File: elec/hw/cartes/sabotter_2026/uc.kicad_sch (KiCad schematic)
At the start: 34 parts, among them J3 USB4105-GF-A-060, SW1 TSB001A3526A02, U3 ESP32-S3-WROOM-1

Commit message: sabotter wip
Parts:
- added R65: 0R, cocotter_resistor:r0603_reflow, symbol cocotter_resistors:R_0R_0603
- added TP7, TP8: TestPoint, cocotter_others:testpoint-THT-0.5mm, symbol cocotter_others:TestPoint
- J3: value USB4105-GF-A-060 -> USB4120-03-C; footprint cocotter_connectors:USB4105 -> cocotter_connectors:USB4120-03-C; symbol cocotter_connectors:USB-TYPE-C-019 -> cocotter_connectors:USB4120-03-C; DIGIKEY_REF 2073-USB4105-GF-A-060TR-ND -> (none); JLC (none) -> C7450621; JLCPCB Part # C2927039 -> (none)
- SW1: value TSB001A3526A02 -> PTS525 SK15 SMTR2 LFS; footprint cocotter_others:TSB001A3526A02 -> cocotter_others:PTS525 SK15 SMTR2 LFS; symbol cocotter_others:TSB001A3526A02 -> cocotter_others:PTS525 SK15 SMTR2 LFS; JLCPCB Part # C2888889 -> C2689599
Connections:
- net EN_ESP32_3v3: now also R65.2; no longer SW1.2
- net GND: now also SW1.A (1); no longer SW1.1, SW1.MP
- net scl_3v3: now also TP8.1
- net sda_3v3: now also TP7.1
- new net: R65.1, SW1.B (2)

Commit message: sabotter wip
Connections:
- net encod_mot0_A_3v3: now also U3.28 (IO35,SPIIO6,GPIO35,FSPID,SUBSPID); no longer U3.32 (IO39,MTCK,GPIO39,CLK_OUT3,SUBSPICS1)
- net encod_mot0_B_3v3: now also U3.17 (IO9,RTC_GPIO9,GPIO9,TOUCH9,ADC1_CH8,FSPIHD,SUBSPIHD); no longer U3.33 (IO40,MTDO,GPIO40,CLK_OUT2)
- net encod_mot1_A_3v3: now also U3.18 (IO10,RTC_GPIO10,GPIO10,TOUCH10,ADC1_CH9,FSPICS0,FSPIIO4,SUBSPICS0); no longer U3.34 (IO41,MTDI,GPIO41,CLK_OUT1)
- net encod_mot1_B_3v3: now also U3.15 (IO3,RTC_GPIO3,GPIO3,TOUCH3,ADC1_CH2); no longer U3.35 (IO42,MTMS,GPIO42)
- net gyro_miso_3v3: now also U3.30 (IO37,SPIDQS,GPIO37,FSPIQ,SUBSPIQ); no longer U3.28 (IO35,SPIIO6,GPIO35,FSPID,SUBSPID)
- net gyro_mosi_3v3: now also U3.31 (IO38,GPIO38,FSPIWP,SUBSPIWP); no longer U3.29 (IO36,SPIIO7,GPIO36,FSPICLK,SUBSPICL)
- net gyro_sck_3v3: now also U3.32 (IO39,MTCK,GPIO39,CLK_OUT3,SUBSPICS1); no longer U3.31 (IO38,GPIO38,FSPIWP,SUBSPIWP)
- net lidar_pwm_3v3: now also U3.35 (IO42,MTMS,GPIO42); no longer U3.15 (IO3,RTC_GPIO3,GPIO3,TOUCH3,ADC1_CH2)
- net scl_3v3: now also U3.34 (IO41,MTDI,GPIO41,CLK_OUT1); no longer U3.18 (IO10,RTC_GPIO10,GPIO10,TOUCH10,ADC1_CH9,FSPICS0,FSPIIO4,SUBSPICS0)
- net sda_3v3: now also U3.33 (IO40,MTDO,GPIO40,CLK_OUT2); no longer U3.17 (IO9,RTC_GPIO9,GPIO9,TOUCH9,ADC1_CH8,FSPIHD,SUBSPIHD)
- net /gyro_cs_3v3: now also U3.29 (IO36,SPIIO7,GPIO36,FSPICLK,SUBSPICL); no longer U3.30 (IO37,SPIDQS,GPIO37,FSPIQ,SUBSPIQ)
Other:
- moved on the sheet: R10, R21, R5, R6, R9, TP7, TP8

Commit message: sabotter ready for first schematic and routing review
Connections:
- net can_rx_3v3: now also U3.18 (IO10,RTC_GPIO10,GPIO10,TOUCH10,ADC1_CH9,FSPICS0,FSPIIO4,SUBSPICS0); no longer U3.19 (IO11,RTC_GPIO11,GPIO11,TOUCH11,FSPID,FSPIIO5,SUBSPID)
- net can_tx_3v3: now also U3.17 (IO9,RTC_GPIO9,GPIO9,TOUCH9,ADC1_CH8,FSPIHD,SUBSPIHD); no longer U3.12 (IO8,RTC_GPIO8,GPIO8,TOUCH8,ADC1_CH7,SUBSPICS1)
- net dir_mot0_3v3: now also U3.11 (IO18,RTC_GPIO18,GPIO18,U1RXD,CLK_OUT3); no longer U3.20 (IO12,RTC_GPIO12,GPIO12,TOUCH12,FSPICLK,FSPIIO6,SUBSPICLK)
- net dir_mot1_3v3: now also U3.12 (IO8,RTC_GPIO8,GPIO8,TOUCH8,ADC1_CH7,SUBSPICS1); no longer U3.22 (IO14,RTC_GPIO14,GPIO14,TOUCH14,FSPIWP,FSPIDQS,SUBSPIWP)
- net dir_mot2_3v3: now also U3.25 (IO48,SPICLK_N_DIFF,GPIO48,SUBSPICLK_N_DIFF); no longer U3.9 (IO16,RTC_GPIO16,GPIO16,U0CTS,XTAL_32K_N)
- net encod_mot0_A_3v3: now also U3.19 (IO11,RTC_GPIO11,GPIO11,TOUCH11,FSPID,FSPIIO5,SUBSPID); no longer U3.28 (IO35,SPIIO6,GPIO35,FSPID,SUBSPID)
- net encod_mot0_B_3v3: now also U3.20 (IO12,RTC_GPIO12,GPIO12,TOUCH12,FSPICLK,FSPIIO6,SUBSPICLK); no longer U3.17 (IO9,RTC_GPIO9,GPIO9,TOUCH9,ADC1_CH8,FSPIHD,SUBSPIHD)
- net encod_mot1_A_3v3: now also U3.9 (IO16,RTC_GPIO16,GPIO16,U0CTS,XTAL_32K_N); no longer U3.18 (IO10,RTC_GPIO10,GPIO10,TOUCH10,ADC1_CH9,FSPICS0,FSPIIO4,SUBSPICS0)
- net encod_mot1_B_3v3: now also U3.8 (IO15,RTC_GPIO15,GPIO15,U0RTS,XTAL_32K_P); no longer U3.15 (IO3,RTC_GPIO3,GPIO3,TOUCH3,ADC1_CH2)
- net encod_mot2_A_3v3: now also U3.22 (IO14,RTC_GPIO14,GPIO14,TOUCH14,FSPIWP,FSPIDQS,SUBSPIWP); no longer U3.24 (IO47,SPICLK_P_DIFF,GPIO47,SUBSPICLK_P_DIFF)
- net encod_mot2_B_3v3: now also U3.21 (IO13,RTC_GPIO13,GPIO13,TOUCH13,FSPIQ,FSPIIO7,SUBSPIQ); no longer U3.25 (IO48,SPICLK_N_DIFF,GPIO48,SUBSPICLK_N_DIFF)
- net pwm_mot0_3v3: now also U3.10 (IO17,RTC_GPIO17,GPIO17,U1TXD); no longer U3.21 (IO13,RTC_GPIO13,GPIO13,TOUCH13,FSPIQ,FSPIIO7,SUBSPIQ)
- net pwm_mot1_3v3: now also U3.15 (IO3,RTC_GPIO3,GPIO3,TOUCH3,ADC1_CH2); no longer U3.8 (IO15,RTC_GPIO15,GPIO15,U0RTS,XTAL_32K_P)
- net pwm_mot2_3v3: now also U3.28 (IO35,SPIIO6,GPIO35,FSPID,SUBSPID); no longer U3.23 (IO21,RTC_GPIO21,GPIO21)
- net scl_tof_3v3: now also U3.24 (IO47,SPICLK_P_DIFF,GPIO47,SUBSPICLK_P_DIFF); no longer U3.11 (IO18,RTC_GPIO18,GPIO18,U1RXD,CLK_OUT3)
- net sda_tof_3v3: now also U3.23 (IO21,RTC_GPIO21,GPIO21); no longer U3.10 (IO17,RTC_GPIO17,GPIO17,U1TXD)
- net tx_to_prop_3v3: now also U3.6 (IO6,RTC_GPIO6,GPIO6,TOUCH6,ADC1_CH5); no longer U3.4 (IO4,RTC_GPIO4,GPIO4,TOUCH4,ADC1_CH3)
- net ws2812_data_3v3: now also U3.4 (IO4,RTC_GPIO4,GPIO4,TOUCH4,ADC1_CH3); no longer U3.6 (IO6,RTC_GPIO6,GPIO6,TOUCH6,ADC1_CH5)
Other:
- moved on the sheet: R10, R11, R12, R14, R15, R5, R6, R7, R8, R9, TP1, TP2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

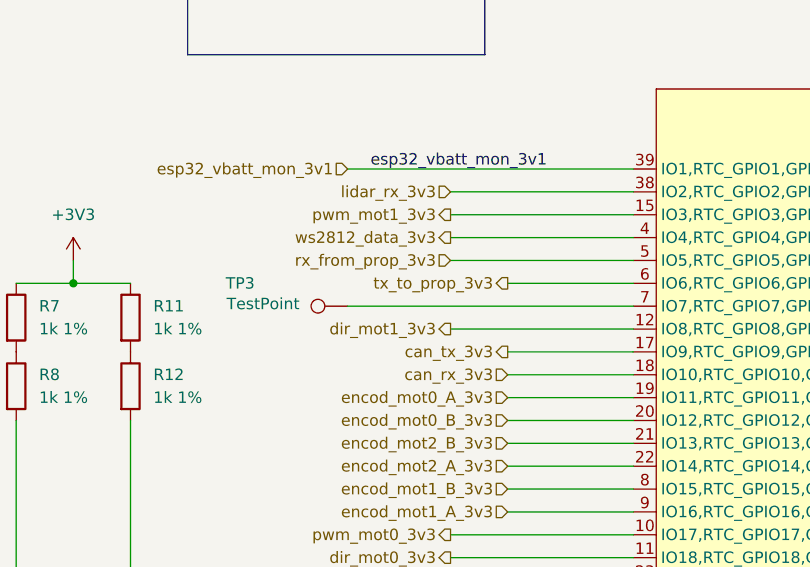
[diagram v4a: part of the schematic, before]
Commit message: tof irq added, needs routing
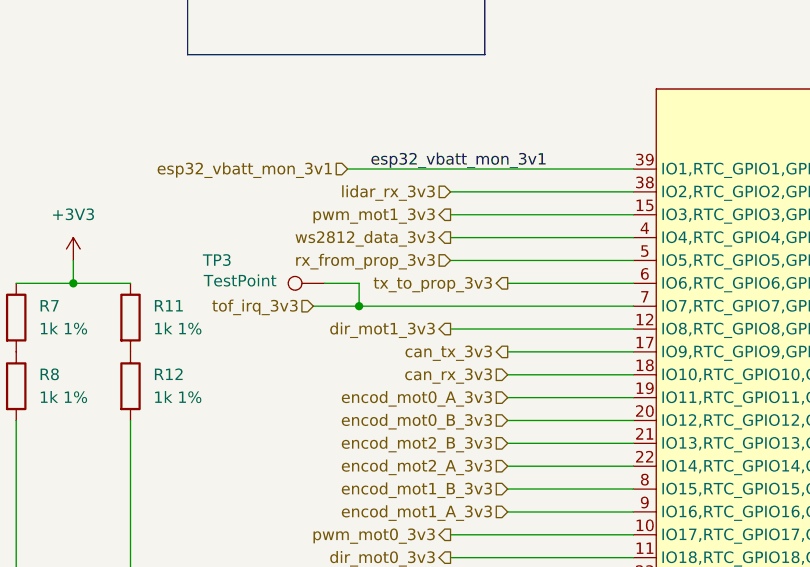
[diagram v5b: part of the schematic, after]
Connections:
- net tof_irq_3v3: now reaches TP3.1, U3.7 (IO7,RTC_GPIO7,GPIO7,TOUCH7,ADC1_CH6)
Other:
- moved on the sheet: TP3
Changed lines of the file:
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@@
 	)
 	(junction
+		(at 104.14 71.12)
+		(diameter 0)
+		(color 0 0 0 0)
+	)
+	(junction
 		(at 30.48 104.14)
 		(diameter 0)
@@
 	(wire
 		(pts
+			(xy 104.14 71.12) (xy 134.62 71.12)
+		)
+		(stroke
+			(width 0)
+			(type default)
+		)
+	)
+	(wire
+		(pts
 			(xy 52.07 100.33) (xy 52.07 101.6)
 		)
@@
 	(wire
 		(pts
+			(xy 99.06 71.12) (xy 104.14 71.12)
+		)
+		(stroke
+			(width 0)
+			(type default)
+		)
+	)
+	(wire
+		(pts
 			(xy 135.89 176.53) (xy 124.46 176.53)
 		)
@@
 	(wire
 		(pts
-			(xy 102.87 71.12) (xy 134.62 71.12)
+			(xy 100.33 68.58) (xy 104.14 68.58)
 		)
 		(stroke
@@
 	(wire
 		(pts
+			(xy 104.14 68.58) (xy 104.14 71.12)
+		)
+		(stroke
+			(width 0)
+			(type default)
+		)
+	)
+	(wire
+		(pts
 			(xy 172.72 148.59) (xy 172.72 149.86)
 		)
@@
 		)
 	)
+	(hierarchical_label "tof_irq_3v3"
+		(shape input)
+		(at 99.06 71.12 180)
+		(effects
+			(font
+				(size 1.27 1.27)
+			)
+			(justify right)
+		)
+	)
 	(hierarchical_label "encod_mot0_A_3v3"
 		(shape input)
@@
 	(symbol
 		(lib_id "cocotter_others:TestPoint")
-		(at 102.87 71.12 90)
+		(at 100.33 68.58 90)
 		(unit 1)
 		(exclude_from_sim no)
@@
 		(dnp no)
 		(property "Reference" "TP3"
-			(at 90.932 68.58 90)
+			(at 88.392 66.04 90)
 			(effects
 				(font
@@
 		)
 		(property "Value" "TestPoint"
-			(at 93.472 70.866 90)
+			(at 90.932 68.326 90)
 			(effects
 				(font
@@
 		)
 		(property "Footprint" "cocotter_others:testpoint-THT-0.5mm"
-			(at 102.87 66.04 0)
+			(at 100.33 63.5 0)
 			(effects
 				(font
@@
 		)
 		(property "Datasheet" "~"
-			(at 102.87 66.04 0)
+			(at 100.33 63.5 0)
 			(effects
 				(font
@@
 		)
 		(property "Description" "test point"
-			(at 102.87 71.12 0)
+			(at 100.33 68.58 0)
 			(effects
 				(font

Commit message: sabotter corrections wip
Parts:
- removed R65: 0R, cocotter_resistor:r0603_reflow, symbol cocotter_resistors:R_0R_0603
- added SW2: SLW-713515-2A-SMT-TR, cocotter_others:SLW-713515-2A-SMT-TR, symbol cocotter_connectors:SLW-713515-2A-SMT-TR
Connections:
- net EN_ESP32_3v3: now also SW2.2
- net at SW1.B (2): now also SW2.1
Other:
- moved on the sheet: SW1
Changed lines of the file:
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@@
 	(wire
 		(pts
-			(xy 69.85 152.4) (xy 69.85 153.67)
+			(xy 57.15 152.4) (xy 57.15 153.67)
 		)
 		(stroke
@@
 	(wire
 		(pts
+			(xy 73.66 143.51) (xy 80.01 143.51)
+		)
+		(stroke
+			(width 0)
+			(type default)
+		)
+	)
+	(wire
+		(pts
 			(xy 231.14 149.86) (xy 231.14 151.13)
 		)
@@
 	(wire
 		(pts
-			(xy 69.85 143.51) (xy 69.85 144.78)
+			(xy 57.15 140.97) (xy 57.15 144.78)
 		)
 		(stroke
@@
 	(wire
 		(pts
-			(xy 78.74 143.51) (xy 80.01 143.51)
-		)
-		(stroke
-			(width 0)
-			(type default)
-		)
-	)
-	(wire
-		(pts
 			(xy 104.14 68.58) (xy 104.14 71.12)
 		)
@@
 	(wire
 		(pts
-			(xy 69.85 143.51) (xy 71.12 143.51)
+			(xy 57.15 140.97) (xy 63.5 140.97)
 		)
 		(stroke
@@
 	)
 	(symbol
-		(lib_id "cocotter_resistors:R_0R_0603")
-		(at 74.93 143.51 90)
-		(unit 1)
-		(exclude_from_sim no)
-		(in_bom yes)
-		(on_board yes)
-		(dnp no)
-		(fields_autoplaced yes)
-		(property "Reference" "R65"
-			(at 74.93 137.16 90)
-			(effects
-				(font
-					(size 1.27 1.27)
-				)
-			)
-		)
-		(property "Value" "0R"
-			(at 74.93 139.7 90)
-			(effects
-				(font
-					(size 1.27 1.27)
-				)
-			)
-		)
-		(property "Footprint" "cocotter_resistor:r0603_reflow"
-			(at 74.93 145.288 90)
-			(effects
-				(font
-					(size 1.27 1.27)
-				)
-				(hide yes)
-			)
-		)
-		(property "Datasheet" "~"
-			(at 74.93 143.51 0)
-			(effects
-				(font
-					(size 1.27 1.27)
-				)
-				(hide yes)
-			)
-		)
-		(property "Description" "Resistor"
-			(at 74.93 143.51 0)
-			(effects
-				(font
-					(size 1.27 1.27)
-				)
-				(hide yes)
-			)
-		)
-		(property "Specification" "0R 0603 20mOhms max 100mW"
-			(at 74.93 143.51 0)
-			(effects
-				(font
-					(size 1.27 1.27)
-				)
-				(hide yes)
-			)
-		)
-		(property "mouser" ""
-			(at 74.93 143.51 0)
-			(effects
-				(font
-					(size 1.27 1.27)
-				)
-				(hide yes)
-			)
-		)
-		(property "JLCPCB Part #" "C431718"
-			(at 74.93 143.51 0)
-			(effects
-				(font
-					(size 1.27 1.27)
-				)
-				(hide yes)
-			)
-		)
-		(pin "1"
-		)
-		(pin "2"
-		)
-		(instances
-			(project ""
-				(path "/c1bd5504-d0b2-4cc3-94d1-261f58816249/0627c134-32e1-430c-bbd1-677b8ecf53c1"
-					(reference "R65")
-					(unit 1)
-				)
-			)
-		)
-	)
-	(symbol
 		(lib_id "pmi_2023_specific:+3V3_m")
 		(at 72.39 66.04 0)
@@
 	(symbol
 		(lib_id "cocotter_others:PTS525 SK15 SMTR2 LFS")
-		(at 69.85 148.59 90)
+		(at 57.15 148.59 90)
 		(unit 1)
 		(exclude_from_sim no)
@@
 		(dnp no)
 		(property "Reference" "SW1"
-			(at 65.278 148.59 0)
+			(at 52.578 148.59 0)
 			(effects
 				(font
@@
 		)
 		(property "Value" "PTS525 SK15 SMTR2 LFS"
-			(at 74.93 146.05 0)
+			(at 62.23 146.05 0)
 			(effects
 				(font
@@
 		)
 		(property "Footprint" "cocotter_others:PTS525 SK15 SMTR2 LFS"
-			(at 69.85 148.59 0)
+			(at 57.15 148.59 0)
 			(effects
 				(font
@@
 		)
 		(property "Datasheet" ""
-			(at 74.93 148.59 0)
+			(at 62.23 148.59 0)
 			(effects
 				(font
@@
 		)
 		(property "Description" "20mA max, 15Vdc, 100mohms max, 500k cycle, 260gf"
-			(at 69.85 148.59 0)
+			(at 57.15 148.59 0)
 			(effects
 				(font
@@
 		)
 		(property "JLCPCB Part #" "C2689599"
-			(at 74.93 149.86 0)
+			(at 62.23 149.86 0)
 			(effects
 				(font
@@
 	)
 	(symbol
+		(lib_id "cocotter_connectors:SLW-713515-2A-SMT-TR ")
+		(at 68.58 143.51 0)
+		(unit 1)
+		(exclude_from_sim no)
+		(in_bom yes)
+		(on_board yes)
+		(dnp no)
+		(fields_autoplaced yes)
+		(property "Reference" "SW2"
+			(at 68.58 134.62 0)
+			(effects
+				(font
+					(size 1.27 1.27)
+				)
+			)
+		)
+		(property "Value" "SLW-713515-2A-SMT-TR"
+			(at 68.58 137.16 0)
+			(effects
+				(font
+					(size 1.27 1.27)
+				)
+			)
+		)
+		(property "Footprint" "cocotter_others:SLW-713515-2A-SMT-TR"
+			(at 68.58 143.51 0)
+			(effects
+				(font
+					(size 1.27 1.27)
+				)
+				(hide yes)
+			)
+		)
+		(property "Datasheet" "https://www.sameskydevices.com/product/resource/slw-713515-2a-smt-tr.pdf"
+			(at 68.58 148.59 0)
+			(effects
+				(font
+					(size 1.27 1.27)
+				)
+				(hide yes)
+			)
+		)
+		(property "Description" "50mA max, 12Vdc, 10000 cycles"
+			(at 68.58 143.51 0)
+			(effects
+				(font
+					(size 1.27 1.27)
+				)
+				(hide yes)
+			)
+		)
+		(property "JLCPCB Part #" "C2858291"
+			(at 67.31 148.59 0)
+			(effects
+				(font
+					(size 1.27 1.27)
+				)
+				(hide yes)
+			)
+		)
+		(pin "2"
+		)
+		(pin "1"
+		)
+		(pin "3"
+		)
+		(pin "6"
+		)
+		(pin "4"
+		)
+		(pin "5"
+		)
+		(instances
+			(project ""
+				(path "/c1bd5504-d0b2-4cc3-94d1-261f58816249/0627c134-32e1-430c-bbd1-677b8ecf53c1"
+					(reference "SW2")
+					(unit 1)
+				)
+			)
+		)
+	)
+	(symbol
 		(lib_id "cocotter_resistors:R_0R_0603")
 		(at 120.65 173.99 90)
@@
 	(symbol
 		(lib_id "pmi_2023_specific:GND_m")
-		(at 69.85 153.67 0)
+		(at 57.15 153.67 0)
 		(unit 1)
 		(exclude_from_sim no)
@@
 		(dnp no)
 		(property "Reference" "#PWR14"
-			(at 69.85 160.02 0)
+			(at 57.15 160.02 0)
 			(effects
 				(font
@@
 		)
 		(property "Value" "GND"
-			(at 69.85 157.48 0)
+			(at 57.15 157.48 0)
 			(effects
 				(font
@@
 		)
 		(property "Footprint" ""
-			(at 69.85 153.67 0)
+			(at 57.15 153.67 0)
 			(effects
 				(font
@@
 		)
 		(property "Datasheet" ""
-			(at 69.85 153.67 0)
+			(at 57.15 153.67 0)
 			(effects
 				(font
@@
 		)
 		(property "Description" "Power symbol creates a global label with name \"GND\" , ground"
-			(at 69.85 153.67 0)
+			(at 57.15 153.67 0)
 			(effects
 				(font

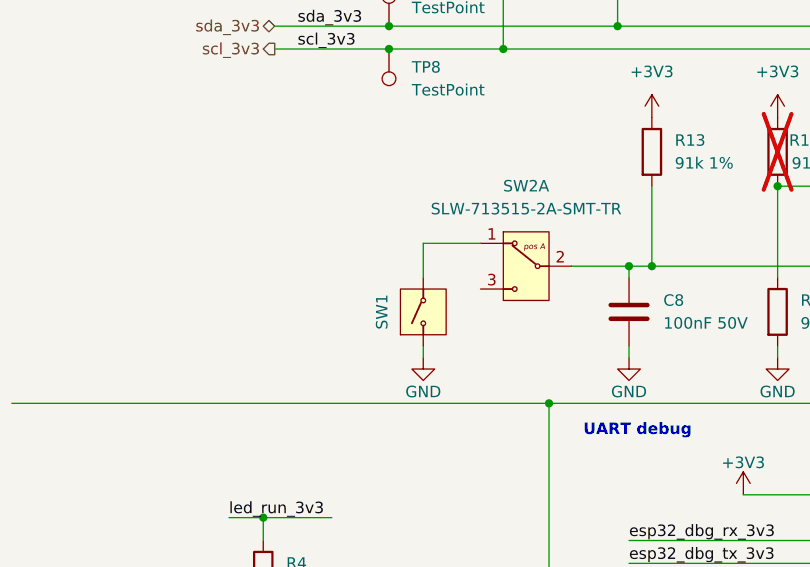
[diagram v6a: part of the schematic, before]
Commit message: sabotter upodate : switch added to uc reset and color selection
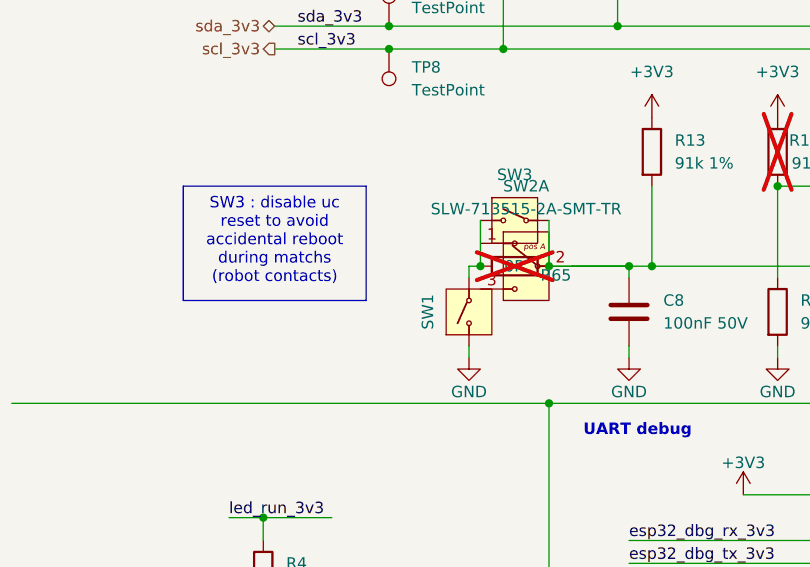
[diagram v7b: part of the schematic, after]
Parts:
- added R65: 0R, cocotter_resistor:r0603_reflow, symbol cocotter_resistors:R_0R_0603
- added SW3: DSIC01LSGER, cocotter_others:DIP_SW_SMD-1P, symbol cocotter_others:DIP_SW_SMD-1P
- SW1: footprint cocotter_others:PTS525 SK15 SMTR2 LFS -> cocotter_others:PTS525
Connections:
- net EN_ESP32_3v3: now also R65.2, SW3.2
- net at SW1.B (2): now also R65.1, SW3.1; no longer SW2.1
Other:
- moved on the sheet: SW1
